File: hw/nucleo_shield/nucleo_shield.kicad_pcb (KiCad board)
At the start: 2 copper layers, 151 x 90.9 mm, 97 parts, among them CN101 Nucleo-F411RE-CN10, CN71 Nucleo-F411RE-CN7, P1 CONN_INH1, P10 CONN_OUTH1, P11 CONN_OUTH2, P12 CONN_RS485_OUT, P13 CONN_RS485_IN, P14 CONN_02X06, P15 CONN_EXT2, P16 CONN_EXTI2C, P17 CONN_INH3, P18 CONN_1WIRE, P19 CONN_EXT_SPI, P2 CONN_OUT3, P20 CON_BME, P21 CON_BH, P3 POWER_24V_CON, P4 POWER_CON, P5 CONN_INH2, P6 ETH_CONN, P7 CONN_LCD_SD, P8 CONN_OUT4, P9 CONN_SCT, U1 74HC595, U10 ULN2803, U11 74HC595, U12 74HC595, U14 PCF8574A, U15 LTV-847, U16 LTV-847, U2 74HC595, U3 LTV-847, U4 LTV-847, U5 LTV-847, U6 LTV-847, U7 PCF8574A, U8 PCF8574A, U9 ULN2803

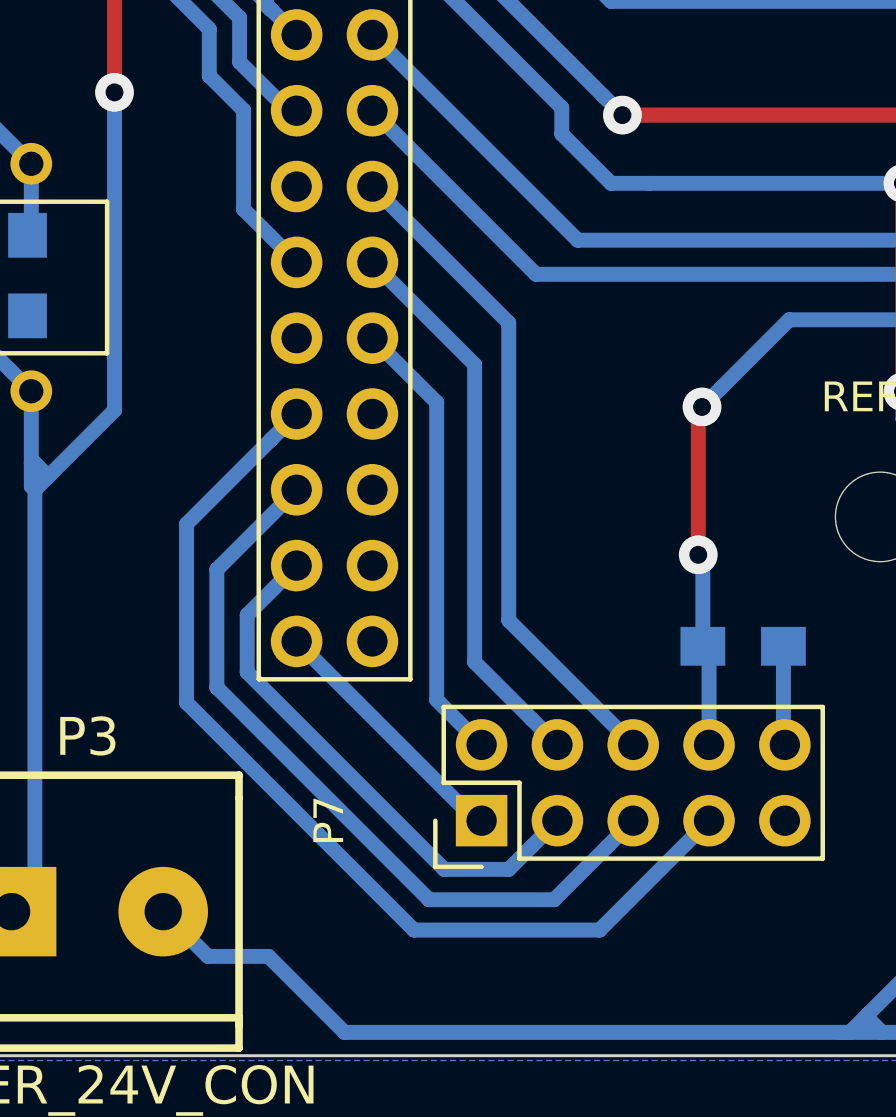
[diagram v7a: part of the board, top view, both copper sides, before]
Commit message: Nucleo: fix pin of uart used as gpio
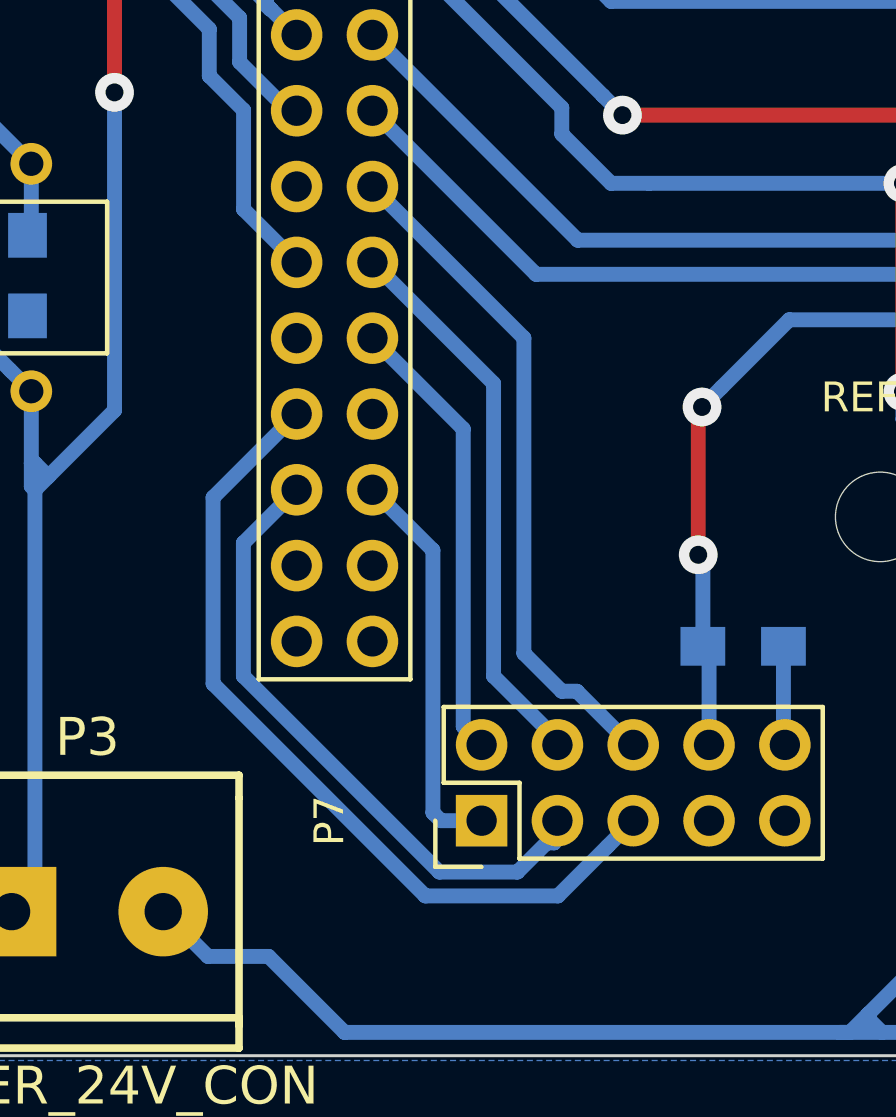
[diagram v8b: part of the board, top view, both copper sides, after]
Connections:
- CN101 pad 29: (no net) -> SD_CS
- CN101 pad 31: SD_CS -> LCD_DC
- CN101 pad 33: LCD_DC -> LCD_RST
- CN101 pad 34: (no net) -> LCD_CS
- CN101 pad 35: LCD_RST -> (no net)
- CN101 pad 37: LCD_CS -> (no net)
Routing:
- net SD_CS: track 33.4 -> 0.00 mm
- net LCD_CS: track 8.69 -> 13.6 mm
- net LCD_RST: track 18.1 -> 21.3 mm
- net LCD_DC: track 25.7 -> 28.3 mm
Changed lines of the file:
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@@
-(kicad_pcb (version 4) (host pcbnew "(after 2015-mar-04 BZR unknown)-product")
+(kicad_pcb (version 4) (host pcbnew "(2016-05-03 BZR 6770, Git 22c4e4d)-product")
   (general
     (links 355)
-    (no_connects 0)
-    (area 82.280379 37.454547 261.1306 159.062401)
+    (no_connects 70)
+    (area 95.072999 57.988999 246.176001 149.021001)
     (thickness 1.6)
     (drawings 9)
-    (tracks 1462)
+    (tracks 1464)
     (zones 0)
     (modules 97)
@@
       (hpglpenspeed 20)
       (hpglpendiameter 15)
-      (hpglpenoverlay 2)
       (psnegative false)
       (psa4output false)
@@
     (pad 28 thru_hole oval (at 2.54 33.02) (size 1.7272 1.7272) (drill 1.016) (layers *.Cu *.Mask F.SilkS)
       (net 72 SPI1_MISO))
-    (pad 29 thru_hole oval (at 0 35.56) (size 1.7272 1.7272) (drill 1.016) (layers *.Cu *.Mask F.SilkS))
+    (pad 29 thru_hole oval (at 0 35.56) (size 1.7272 1.7272) (drill 1.016) (layers *.Cu *.Mask F.SilkS)
+      (net 74 SD_CS))
     (pad 30 thru_hole oval (at 2.54 35.56) (size 1.7272 1.7272) (drill 1.016) (layers *.Cu *.Mask F.SilkS)
       (net 71 SPI1_SCK))
     (pad 31 thru_hole oval (at 0 38.1) (size 1.7272 1.7272) (drill 1.016) (layers *.Cu *.Mask F.SilkS)
-      (net 74 SD_CS))
+      (net 77 LCD_DC))
     (pad 32 thru_hole oval (at 2.54 38.1) (size 1.7272 1.7272) (drill 1.016) (layers *.Cu *.Mask F.SilkS))
     (pad 33 thru_hole oval (at 0 40.64) (size 1.7272 1.7272) (drill 1.016) (layers *.Cu *.Mask F.SilkS)
-      (net 77 LCD_DC))
-    (pad 34 thru_hole oval (at 2.54 40.64) (size 1.7272 1.7272) (drill 1.016) (layers *.Cu *.Mask F.SilkS))
-    (pad 35 thru_hole oval (at 0 43.18) (size 1.7272 1.7272) (drill 1.016) (layers *.Cu *.Mask F.SilkS)
       (net 76 LCD_RST))
-    (pad 36 thru_hole oval (at 2.54 43.18) (size 1.7272 1.7272) (drill 1.016) (layers *.Cu *.Mask F.SilkS))
-    (pad 37 thru_hole oval (at 0 45.72) (size 1.7272 1.7272) (drill 1.016) (layers *.Cu *.Mask F.SilkS)
+    (pad 34 thru_hole oval (at 2.54 40.64) (size 1.7272 1.7272) (drill 1.016) (layers *.Cu *.Mask F.SilkS)
       (net 75 LCD_CS))
+    (pad 35 thru_hole oval (at 0 43.18) (size 1.7272 1.7272) (drill 1.016) (layers *.Cu *.Mask F.SilkS))
+    (pad 36 thru_hole oval (at 2.54 43.18) (size 1.7272 1.7272) (drill 1.016) (layers *.Cu *.Mask F.SilkS))
+    (pad 37 thru_hole oval (at 0 45.72) (size 1.7272 1.7272) (drill 1.016) (layers *.Cu *.Mask F.SilkS))
     (pad 38 thru_hole oval (at 2.54 45.72) (size 1.7272 1.7272) (drill 1.016) (layers *.Cu *.Mask F.SilkS))
     (model Pin_Headers.3dshapes/Pin_Header_Straight_2x19.wrl
@@
   (segment (start 190.0301 94.869) (end 191.5356 96.3745) (width 0.5) (layer B.Cu) (net 70))
   (segment (start 189.484 94.869) (end 190.0301 94.869) (width 0.5) (layer B.Cu) (net 70))
-  (segment (start 184.4236 137.0526) (end 185.928 138.557) (width 0.5) (layer B.Cu) (net 71))
-  (segment (start 184.4236 127.0831) (end 184.4236 137.0526) (width 0.5) (layer B.Cu) (net 71))
-  (segment (start 182.2704 124.9299) (end 184.4236 127.0831) (width 0.5) (layer B.Cu) (net 71))
-  (segment (start 187.604401 137.693401) (end 188.468 138.557) (width 0.5) (layer B.Cu) (net 72))
-  (segment (start 185.6936 135.7826) (end 187.604401 137.693401) (width 0.5) (layer B.Cu) (net 72))
-  (segment (start 185.6936 125.8131) (end 185.6936 135.7826) (width 0.5) (layer B.Cu) (net 72))
-  (segment (start 182.2704 122.3899) (end 185.6936 125.8131) (width 0.5) (layer B.Cu) (net 72))
-  (segment (start 186.8366 124.4161) (end 186.8366 134.3856) (width 0.5) (layer B.Cu) (net 73))
-  (segment (start 186.8366 134.3856) (end 191.008 138.557) (width 0.5) (layer B.Cu) (net 73))
-  (segment (start 182.2704 119.8499) (end 186.8366 124.4161) (width 0.5) (layer B.Cu) (net 73))
-  (segment (start 178.866801 128.333499) (end 179.7304 127.4699) (width 0.5) (layer B.Cu) (net 74))
-  (segment (start 176.0416 137.1415) (end 176.0416 131.1587) (width 0.5) (layer B.Cu) (net 74))
-  (segment (start 189.8835 144.7615) (end 183.6616 144.7615) (width 0.5) (layer B.Cu) (net 74))
-  (segment (start 176.0416 131.1587) (end 178.866801 128.333499) (width 0.5) (layer B.Cu) (net 74))
-  (segment (start 183.6616 144.7615) (end 176.0416 137.1415) (width 0.5) (layer B.Cu) (net 74))
-  (segment (start 193.548 141.097) (end 189.8835 144.7615) (width 0.5) (layer B.Cu) (net 74))
+  (segment (start 185.3126 137.9416) (end 185.928 138.557) (width 0.5) (layer B.Cu) (net 71))
+  (segment (start 182.2704 124.9299) (end 185.3126 127.9721) (width 0.5) (layer B.Cu) (net 71))
+  (segment (start 185.3126 127.9721) (end 185.3126 137.9416) (width 0.5) (layer B.Cu) (net 71))
+  (segment (start 182.2704 122.3899) (end 186.3286 126.4481) (width 0.5) (layer B.Cu) (net 72))
+  (segment (start 186.3286 126.4481) (end 186.3286 136.2525) (width 0.5) (layer B.Cu) (net 72))
+  (segment (start 186.3286 136.2525) (end 188.468 138.3919) (width 0.5) (layer B.Cu) (net 72))
+  (segment (start 188.468 138.3919) (end 188.468 138.557) (width 0.5) (layer B.Cu) (net 72))
+  (segment (start 182.2704 119.8499) (end 187.3446 124.9241) (width 0.5) (layer B.Cu) (net 73))
+  (segment (start 187.3446 124.9241) (end 187.3446 135.4905) (width 0.5) (layer B.Cu) (net 73))
+  (segment (start 187.3446 135.4905) (end 188.6146 136.7605) (width 0.5) (layer B.Cu) (net 73))
+  (segment (start 188.6146 136.7605) (end 189.1226 136.7605) (width 0.5) (layer B.Cu) (net 73))
+  (segment (start 189.1226 136.7605) (end 190.9191 138.557) (width 0.5) (layer B.Cu) (net 73))
+  (segment (start 190.9191 138.557) (end 191.008 138.557) (width 0.5) (layer B.Cu) (net 73))
+  (segment (start 182.2704 130.0099) (end 184.2966 132.0361) (width 0.5) (layer B.Cu) (net 75))
+  (segment (start 184.2966 132.0361) (end 184.2966 140.8292) (width 0.5) (layer B.Cu) (net 75))
+  (segment (start 184.2966 140.8292) (end 184.5644 141.097) (width 0.5) (layer B.Cu) (net 75))
+  (segment (start 184.5644 141.097) (end 185.928 141.097) (width 0.5) (layer B.Cu) (net 75))
   (segment (start 185.7375 141.097) (end 185.928 141.097) (width 0.5) (layer B.Cu) (net 75))
-  (segment (start 179.7304 135.0899) (end 185.7375 141.097) (width 0.5) (layer B.Cu) (net 75))
-  (segment (start 187.604401 141.960599) (end 188.468 141.097) (width 0.5) (layer B.Cu) (net 76))
-  (segment (start 186.8355 142.7295) (end 187.604401 141.960599) (width 0.5) (layer B.Cu) (net 76))
-  (segment (start 178.0736 136.1255) (end 184.6776 142.7295) (width 0.5) (layer B.Cu) (net 76))
-  (segment (start 178.0736 134.2067) (end 178.0736 136.1255) (width 0.5) (layer B.Cu) (net 76))
-  (segment (start 179.7304 132.5499) (end 178.0736 134.2067) (width 0.5) (layer B.Cu) (net 76))
-  (segment (start 184.6776 142.7295) (end 186.8355 142.7295) (width 0.5) (layer B.Cu) (net 76))
-  (segment (start 188.3595 143.7455) (end 190.144401 141.960599) (width 0.5) (layer B.Cu) (net 77))
-  (segment (start 177.0576 136.6335) (end 184.1696 143.7455) (width 0.5) (layer B.Cu) (net 77))
+  (segment (start 179.7304 130.0099) (end 177.9466 131.7937) (width 0.5) (layer B.Cu) (net 76))
+  (segment (start 177.9466 131.7937) (end 177.9466 136.2525) (width 0.5) (layer B.Cu) (net 76))
+  (segment (start 177.9466 136.2525) (end 184.512589 142.818489) (width 0.5) (layer B.Cu) (net 76))
+  (segment (start 184.512589 142.818489) (end 187.128611 142.818489) (width 0.5) (layer B.Cu) (net 76))
+  (segment (start 187.128611 142.818489) (end 188.1066 141.8405) (width 0.5) (layer B.Cu) (net 76))
+  (segment (start 188.1066 141.8405) (end 188.3606 141.8405) (width 0.5) (layer B.Cu) (net 76))
+  (segment (start 188.3606 141.8405) (end 188.3606 141.2044) (width 0.5) (layer B.Cu) (net 76))
+  (segment (start 188.3606 141.2044) (end 188.468 141.097) (width 0.5) (layer B.Cu) (net 76))
+  (segment (start 184.0426 143.6185) (end 188.4865 143.6185) (width 0.5) (layer B.Cu) (net 77))
+  (segment (start 176.9306 136.5065) (end 184.0426 143.6185) (width 0.5) (layer B.Cu) (net 77))
+  (segment (start 179.7304 127.4699) (end 176.9306 130.2697) (width 0.5) (layer B.Cu) (net 77))
+  (segment (start 176.9306 130.2697) (end 176.9306 136.5065) (width 0.5) (layer B.Cu) (net 77))
+  (segment (start 188.4865 143.6185) (end 190.144401 141.960599) (width 0.5) (layer B.Cu) (net 77))
   (segment (start 190.144401 141.960599) (end 191.008 141.097) (width 0.5) (layer B.Cu) (net 77))
-  (segment (start 179.7304 130.0099) (end 177.0576 132.6827) (width 0.5) (layer B.Cu) (net 77))
-  (segment (start 177.0576 132.6827) (end 177.0576 136.6335) (width 0.5) (layer B.Cu) (net 77))
-  (segment (start 184.1696 143.7455) (end 188.3595 143.7455) (width 0.5) (layer B.Cu) (net 77))
   (segment (start 170.9039 91.0844) (end 170.8404 91.1479) (width 0.5) (layer B.Cu) (net 78))
   (segment (start 170.225 90.5325) (end 170.8404 91.1479) (width 0.5) (layer B.Cu) (net 78))
@@
     (connect_pads (clearance 0.508))
     (min_thickness 0.254)
-    (fill yes (arc_segments 16) (thermal_gap 0.508) (thermal_bridge_width 0.508))
+    (fill (arc_segments 16) (thermal_gap 0.508) (thermal_bridge_width 0.508))
     (polygon
       (pts
